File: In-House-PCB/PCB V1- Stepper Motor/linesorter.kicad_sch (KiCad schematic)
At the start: 75 parts, among them J1 USB_A, J10 Sens6, J11 B4B-XH-A LFSN, J12 USB_A, J13 B3B-XH-ALFSN, J14 B3B-XH-ALFSN, J15 B3B-XH-ALFSN, J16 B3B-XH-ALFSN, J17 1985234, J2 B3B-XH-ALFSN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

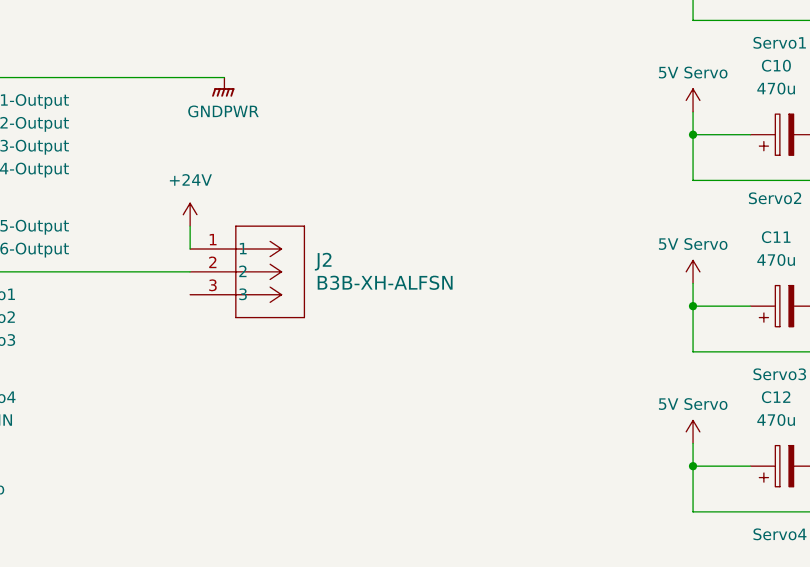
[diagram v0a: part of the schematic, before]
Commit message: Updated Files to be compatible with JLCPCB
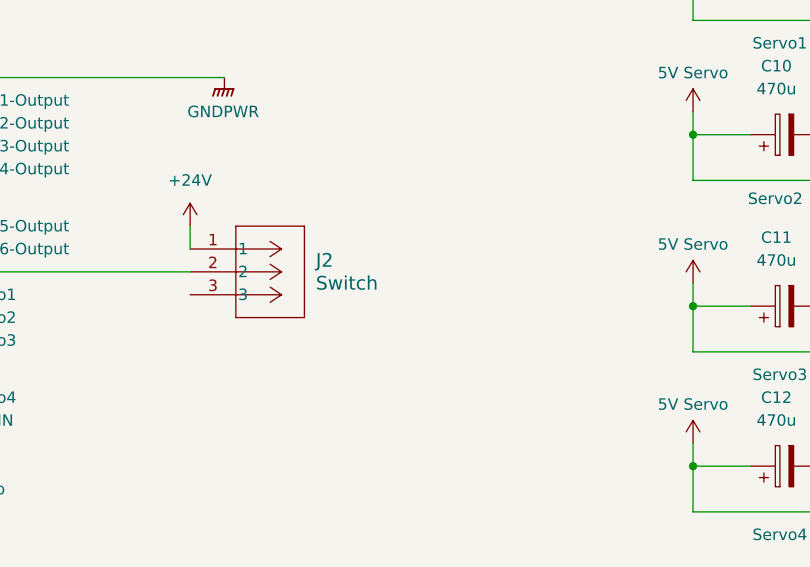
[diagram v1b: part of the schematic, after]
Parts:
- J2: value B3B-XH-ALFSN -> Switch
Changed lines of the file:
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@@
 			)
 		)
-		(property "Value" "B3B-XH-ALFSN"
+		(property "Value" "Switch"
 			(at 80.01 91.4399 0)
 			(effects
